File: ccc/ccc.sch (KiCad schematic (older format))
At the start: 3 parts, among them J1 Conn_02x03_Odd_Even, U1 rt9013-33, U2 LTC3225

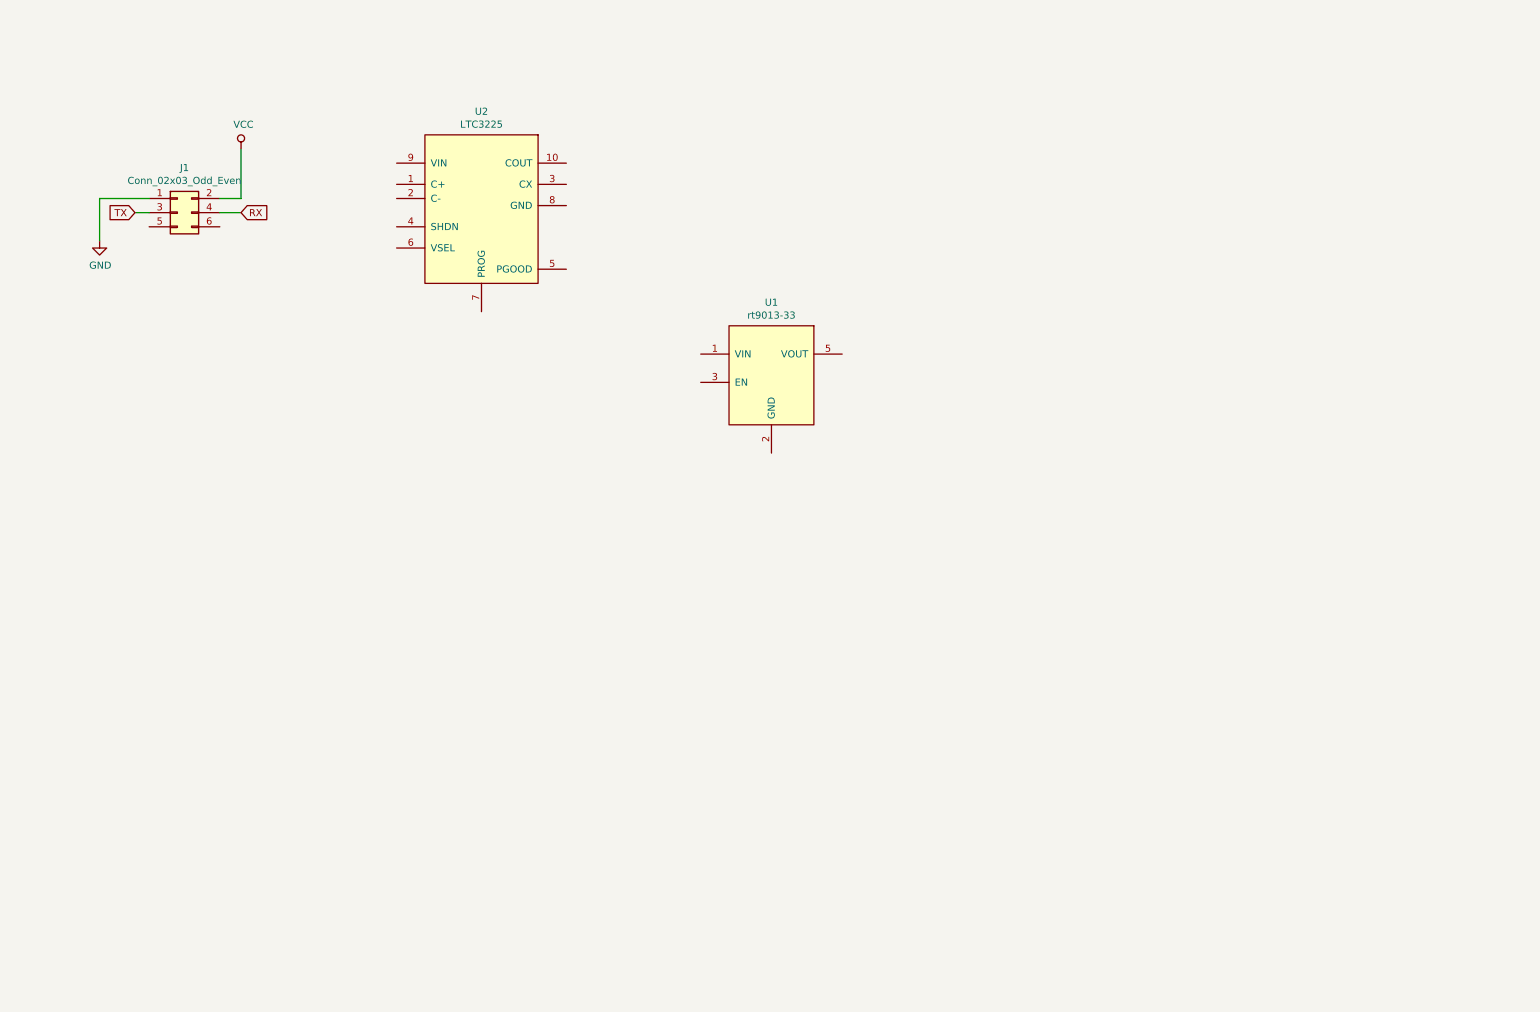
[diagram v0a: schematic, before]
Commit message: Some what prototype with esp8266 which cannot be programmed
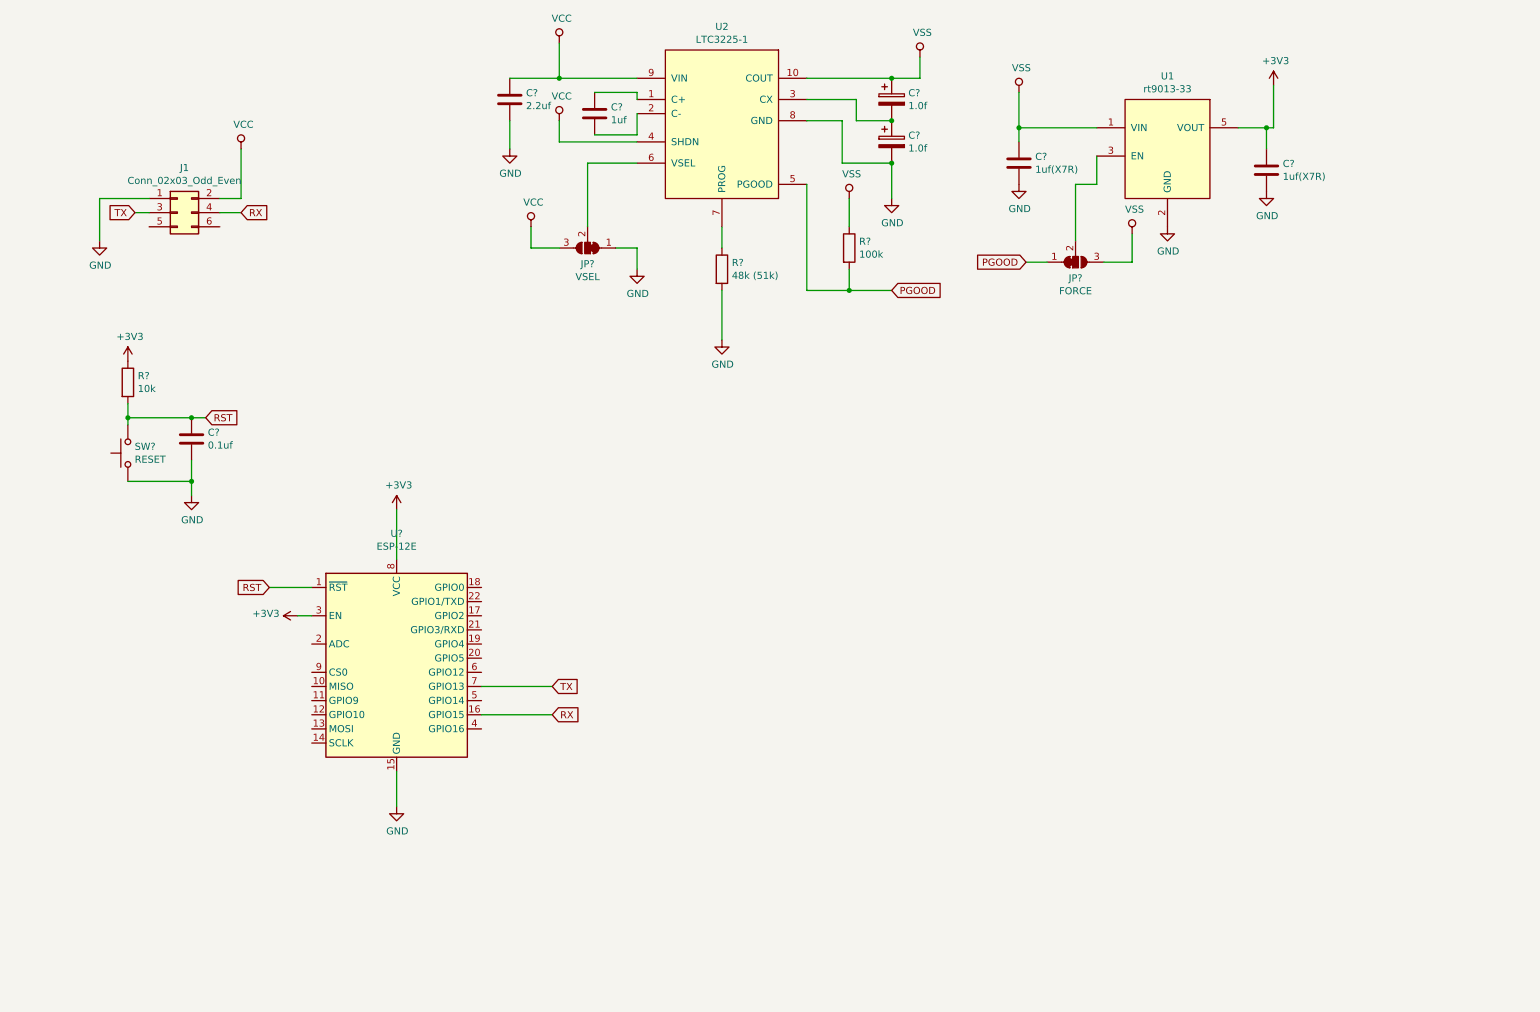
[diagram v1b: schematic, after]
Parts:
- added C?: 2.2uf, symbol Device:C
- added C?: 1uf, symbol Device:C
- added C? (x2): 1.0f, symbol Device:CP
- added C? (x2): 1uf(X7R), symbol Device:C
- added C?: 0.1uf, symbol Device:C
- added JP?: VSEL, symbol Jumper:SolderJumper_3_Bridged12
- added JP?: FORCE, symbol Jumper:SolderJumper_3_Bridged12
- added R?: 48k (51k), symbol Device:R
- added R?: 100k, symbol Device:R
- added R?: 10k, symbol Device:R
- added SW?: RESET, symbol Switch:SW_Push
- added U?: ESP-12E, RF_Module:ESP-12E, symbol RF_Module:ESP-12E
- U2: value LTC3225 -> LTC3225-1
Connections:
- net GND: now also U1.2 (GND), U2.8 (GND), C?.2, C?.2, C?.2, C?.2, C?.2, JP?.1 (A), R?.2, SW?.1, U?.15 (GND)
- net RX: now also U?.16 (GPIO15)
- net TX: now also U?.7 (GPIO13)
- net VCC: now also U2.4 (SHDN), U2.9 (VIN), C?.1, JP?.3 (B)
- net VSS: now reaches U1.1 (VIN)
- net VSS: now also U2.10 (COUT), C?.1, C?.1, JP?.3 (B), R?.1
- net at U1.3 (EN): now also JP?.2 (C)
- net +3V3: now reaches U1.5 (VOUT)
- net +3V3: now also C?.1, R?.1, U?.3 (EN), U?.8 (VCC)
- net at U2.1 (C+): now also C?.1
- net at U2.2 (C-): now also C?.2
- net at U2.3 (CX): now also C?.1, C?.2
- net PGOOD: now reaches U2.5 (PGOOD)
- net PGOOD: now also JP?.1 (A), R?.2
- net at U2.6 (VSEL): now also JP?.2 (C)
- net at U2.7 (PROG): now also R?.1
- new net RST: C?.1, R?.2, SW?.2, U?.1 (~RST)
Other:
- moved on the sheet: U1, U2

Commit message: Added cp2102n datasheet
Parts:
- added J?: USB_B_Micro, symbol Connector:USB_B_Micro
- added U?: ESP32-WROOM-32, RF_Module:ESP32-WROOM-32, symbol RF_Module:ESP32-WROOM-32
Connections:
- net GND: now also U?.1 (GND), U?.15 (GND), U?.38 (GND)
- net RST: now also U?.3 (EN)
- net RX: now also U?.28 (IO17)
- net TX: now also U?.27 (IO16)
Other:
- note added: "Default enable on logic high PGOOD"
- note added: "Default to 4.0v VSS"
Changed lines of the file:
@@
 Wire Wire Line
 	4400 5700 3900 5700
+$Comp
+L RF_Module:ESP32-WROOM-32 U?
+U 1 1 5CE63B00
+P 8800 4800
+F 0 "U?" H 8800 6381 50  0000 C CNN
+F 1 "ESP32-WROOM-32" H 8800 6290 50  0000 C CNN
+F 2 "RF_Module:ESP32-WROOM-32" H 8800 3300 50  0001 C CNN
+F 3 "https://www.espressif.com/sites/default/files/documentation/esp32-wroom-32_datasheet_en.pdf" H 8500 4850 50  0001 C CNN
+	1    8800 4800
+	1    0    0    -1
+$EndComp
+Text GLabel 7950 3600 0    50   Input ~ 0
+RST
+Wire Wire Line
+	7950 3600 8200 3600
+Text GLabel 9750 4700 2    50   Input ~ 0
+RX
+Wire Wire Line
+	9750 4700 9400 4700
+Text GLabel 9750 4500 2    50   Input ~ 0
+TX
+Wire Wire Line
+	9750 4500 9700 4500
+Wire Wire Line
+	9700 4500 9700 4600
+Wire Wire Line
+	9700 4600 9400 4600
+$Comp
+L power:GND #PWR?
+U 1 1 5CE6F95F
+P 8800 6300
+F 0 "#PWR?" H 8800 6050 50  0001 C CNN
+F 1 "GND" H 8805 6127 50  0000 C CNN
+F 2 "" H 8800 6300 50  0001 C CNN
+F 3 "" H 8800 6300 50  0001 C CNN
+	1    8800 6300
+	1    0    0    -1
+$EndComp
+Wire Wire Line
+	8800 6300 8800 6200
+Text Notes 4100 2750 0    50   ~ 0
+Default to 4.0v VSS
+Text Notes 7650 2800 0    50   ~ 0
+Default enable on logic high PGOOD
+$Comp
+L Connector:USB_B_Micro J?
+U 1 1 5CE895CD
+P 5600 4450
+F 0 "J?" H 5657 4917 50  0000 C CNN
+F 1 "USB_B_Micro" H 5657 4826 50  0000 C CNN
+F 2 "" H 5750 4400 50  0001 C CNN
+F 3 "~" H 5750 4400 50  0001 C CNN
+	1    5600 4450
+	1    0    0    -1
+$EndComp
 $EndSCHEMATC

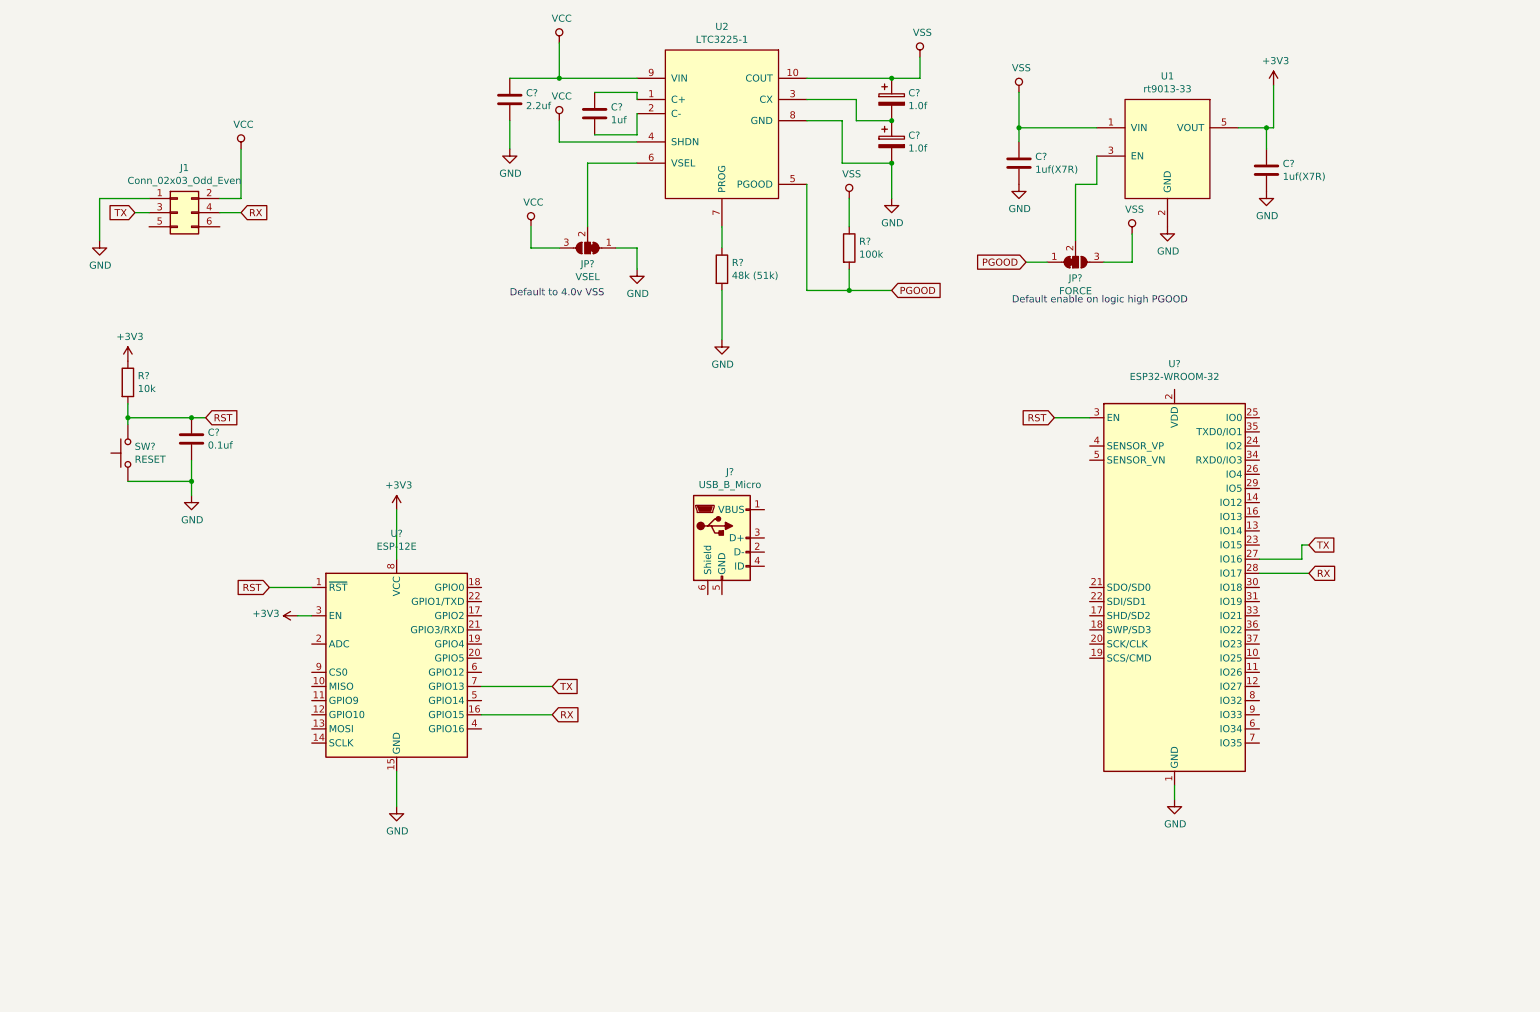
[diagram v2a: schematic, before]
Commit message: Added usb to uart bridge
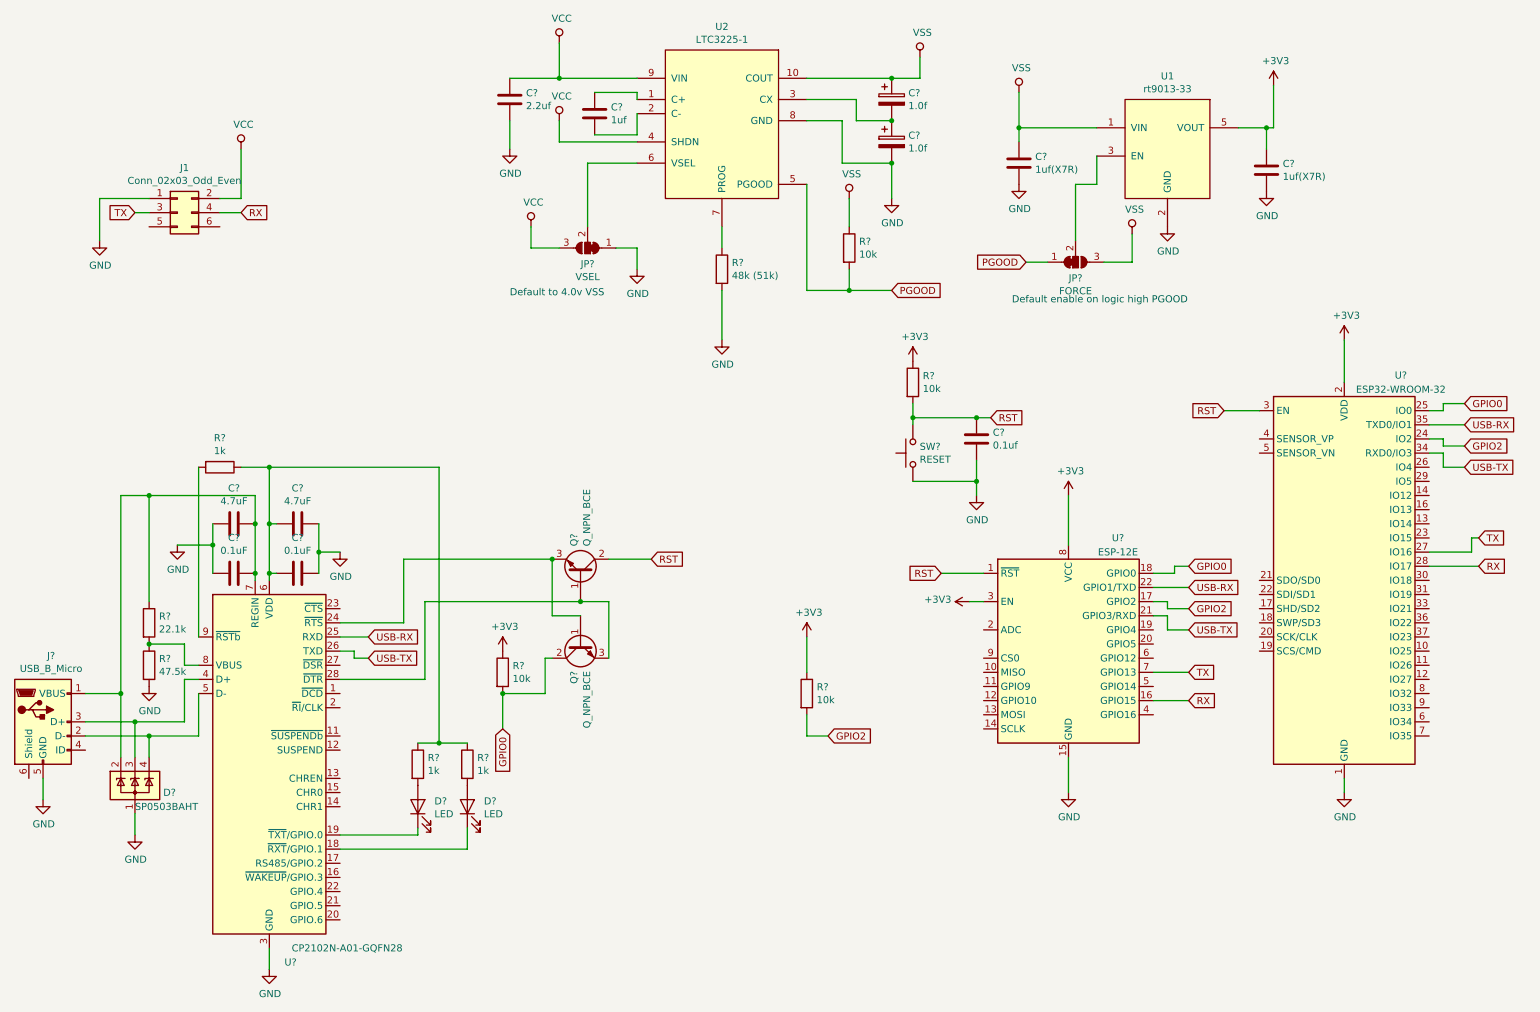
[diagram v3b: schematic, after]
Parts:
- removed J?: USB_B_Micro, symbol Connector:USB_B_Micro
- added C? (x2): 0.1uF, symbol Device:C
- added C? (x2): 4.7uF, symbol Device:C
- added D?: SP0503BAHT, Package_TO_SOT_SMD:SOT-143, symbol Power_Protection:SP0503BAHT
- added D? (x2): LED, symbol Device:LED
- added J?: USB_B_Micro, symbol Connector:USB_B_Micro
- added Q? (x2): Q_NPN_BCE, symbol Device:Q_NPN_BCE
- added R?: 22.1k, symbol Device:R
- added R?: 47.5k, symbol Device:R
- added R? (x3): 1k, symbol Device:R
- added R? (x2): 10k, symbol Device:R
- added U?: CP2102N-A01-GQFN28, Package_DFN_QFN:QFN-28-1EP_5x5mm_P0.5mm_EP3.35x3.35mm, symbol Interface_USB:CP2102N-A01-GQFN28
- R?: value 100k -> 10k
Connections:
- net +3V3: now also U?.2 (VDD), R?.1, R?.1
- net GND: now also C?.1, C?.1, C?.2, C?.2, D?.1 (A), J?.5 (GND), R?.2, U?.29 (GND), U?.3 (GND)
- net RST: now also Q?.2 (C)
- net GPIO2: now reaches U?.17 (GPIO2)
- net GPIO2: now also U?.24 (IO2), R?.2
- net GPIO0: now reaches U?.18 (GPIO0)
- net GPIO0: now also U?.25 (IO0), Q?.2 (C), R?.2
- net USB-TX: now reaches U?.21 (GPIO3/RXD)
- net USB-TX: now also U?.34 (RXD0/IO3), U?.26 (TXD)
- net USB-RX: now reaches U?.22 (GPIO1/TXD)
- net USB-RX: now also U?.35 (TXD0/IO1), U?.25 (RXD)
- new net: C?.1, C?.1, D?.2 (K), J?.1 (VBUS), R?.1, U?.7 (REGIN)
- new net: D?.4 (K), J?.2 (D-), U?.5 (D-)
- new net: D?.3 (K), J?.3 (D+), U?.4 (D+)
- new net: D?.1 (K), U?.18 (~RXT~/GPIO.1)
- new net: D?.1 (K), U?.19 (~TXT~/GPIO.0)
- new net: Q?.1 (B), Q?.3 (E), U?.24 (~RTS)
- new net: Q?.1 (B), Q?.3 (E), U?.28 (~DTR)
- new net: C?.2, C?.2, R?.1, R?.1, R?.1, U?.6 (VDD)
- new net: R?.1, R?.2, U?.8 (VBUS)
- new net: R?.2, U?.9 (~RSTb)
- new net: D?.2 (A), R?.2 (x2)
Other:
- moved on the sheet: C?, R?, SW?, U?
